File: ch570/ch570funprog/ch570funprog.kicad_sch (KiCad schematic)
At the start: 19 parts, among them J1 DEVPGM, J2 USB_C_Receptacle_USB2.0, J3 COREPGM, U1 USBLC6-2SC6, U2 CH570Q, U3 AMS1117-3.3, U4 DMC2400UV, Y1 32M

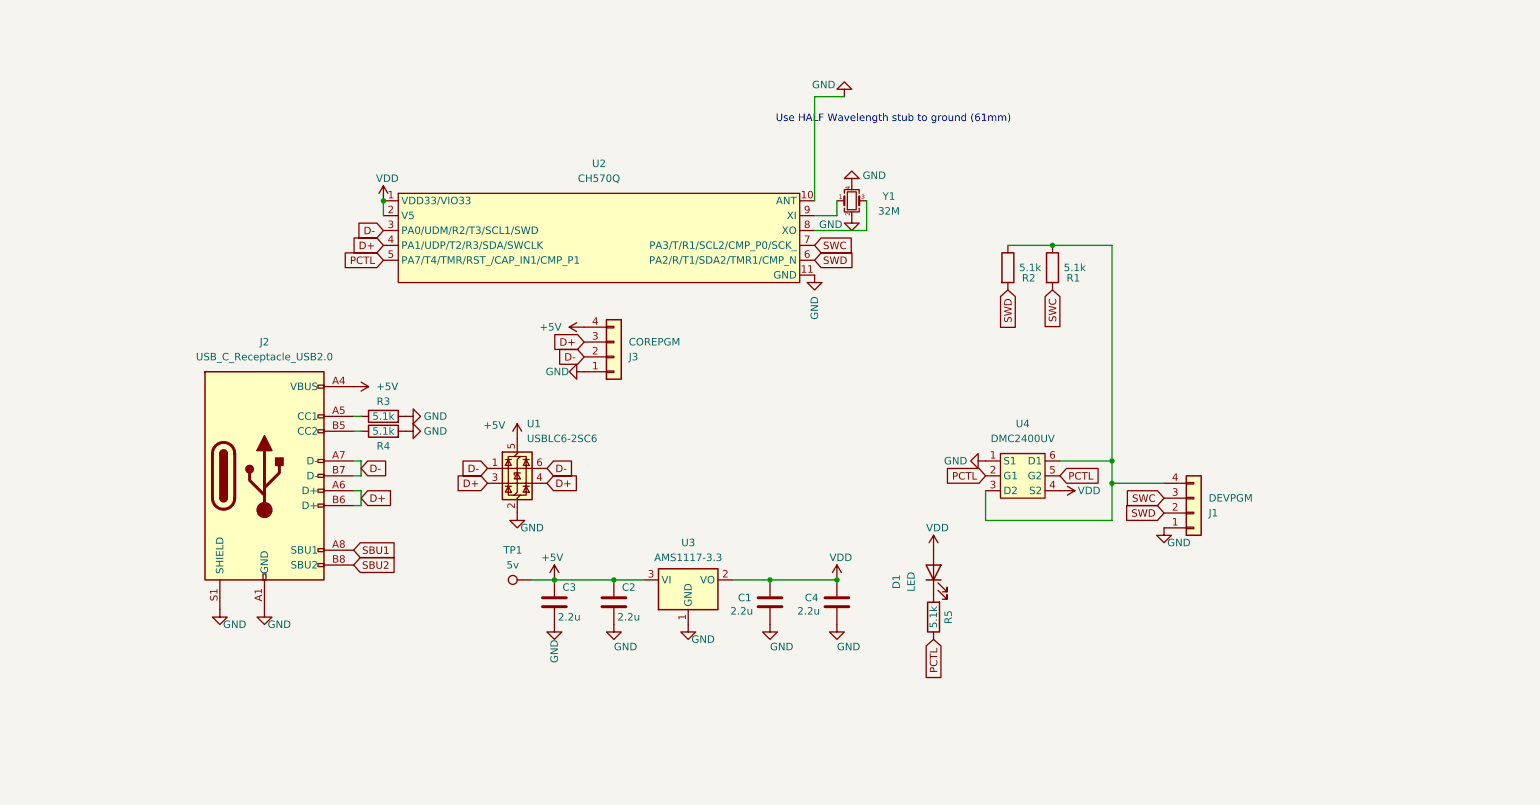
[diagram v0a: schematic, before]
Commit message: Bump design workAnd properly name polypsec
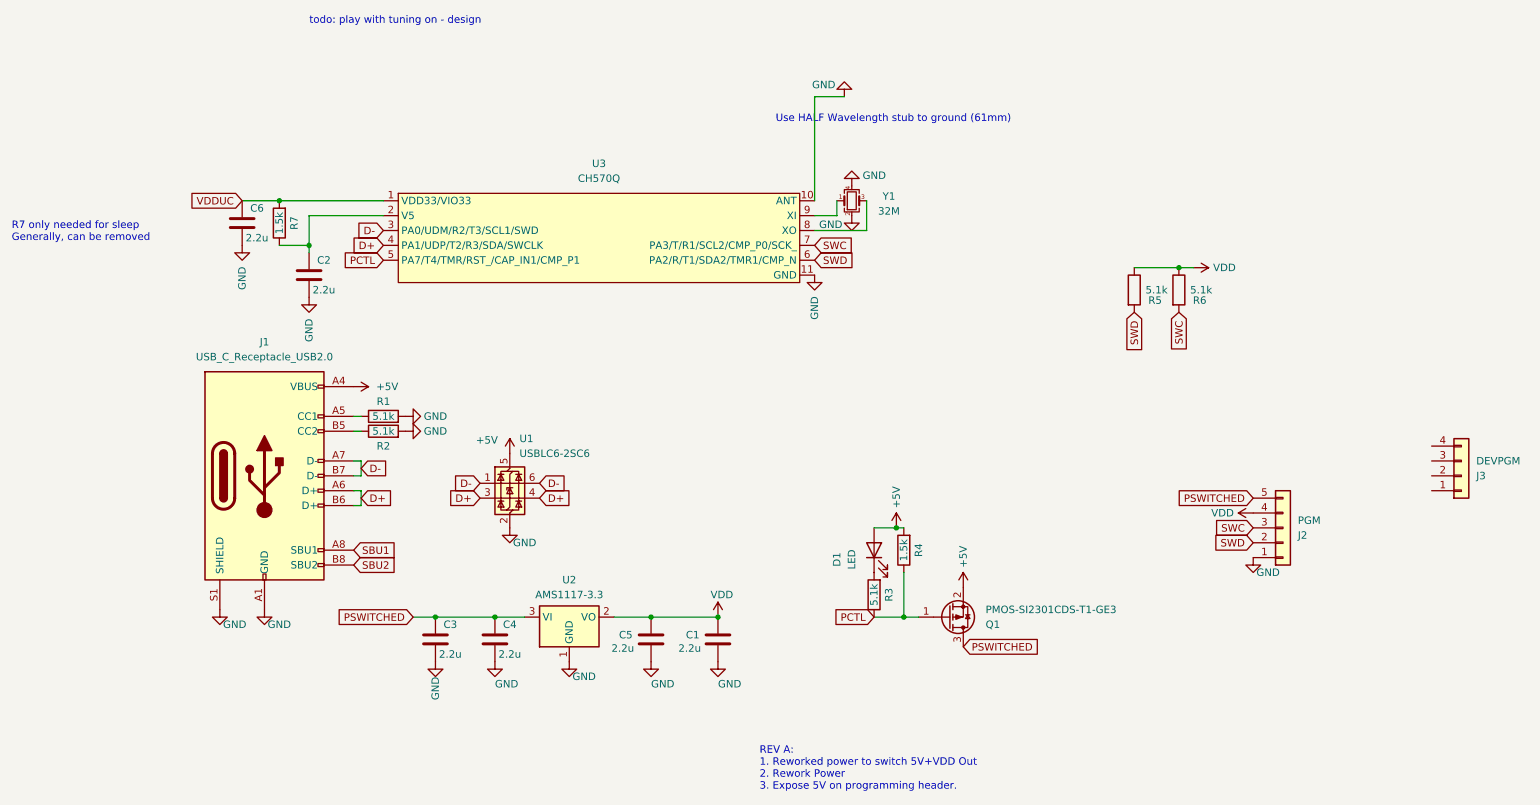
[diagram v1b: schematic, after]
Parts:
- removed J3: COREPGM, Connector_PinHeader_2.54mm:PinHeader_1x04_P2.54mm_Vertical, symbol Connector_Generic:Conn_01x04
- removed TP1: 5v, TestPoint:TestPoint_Pad_D1.5mm, symbol Connector:TestPoint
- removed U4: DMC2400UV, Package_TO_SOT_SMD:SOT-563, symbol cnhardware:DMC2400UV_COMPLEMENTARY_PAIR_FET
- added C2, C6: 2.2u, Resistor_SMD:R_0402_1005Metric, symbol Device:C
- added J2: PGM, Connector_PinHeader_2.54mm:PinHeader_1x05_P2.54mm_Horizontal, symbol Connector_Generic:Conn_01x05
- added Q1: PMOS-SI2301CDS-T1-GE3, Package_TO_SOT_SMD:SOT-23, symbol Transistor_FET:Q_PMOS_GSD
- added R4, R7: 1.5k, Resistor_SMD:R_0402_1005Metric, symbol Device:R
- renumbered C4 to C1, C2 to C4, C1 to C5, J2 to J1, J1 to J3, R3 to R1, R4 to R2, R5 to R3, R2 to R5, R1 to R6, U3 to U2, U2 to U3
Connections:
- net +5V: now also D1.2 (A), Q1.2 (S), R4.2; no longer C3.2, C4.2, U2.3 (VI)
- net GND: now also C2.1, C6.1, J2.1 (Pin_1); no longer J3.1 (Pin_1)
- net PCTL: now also Q1.1 (G), R4.1
- net SWC: now also J2.3 (Pin_3); no longer J3.3 (Pin_3)
- net SWD: now also J2.2 (Pin_2); no longer J3.2 (Pin_2)
- net VDD: now also R5.1, R6.1, J2.4 (Pin_4); no longer D1.2 (A), U3.1 (VDD33/VIO33), U3.2 (V5)
- new net: C2.2, R7.1, U3.2 (V5)
- new net PSWITCHED: C3.2, C4.2, J2.5 (Pin_5), Q1.3 (D), U2.3 (VI)
- new net VDDUC: C6.2, R7.2, U3.1 (VDD33/VIO33)
- now unconnected: J3.4 (Pin_4)
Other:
- note added: "R7 only needed for sleep Generally, can be removed"
- note added: "REV A: 1. Reworked power to switch 5V+VDD Out 2. Rework Power 3. Expose 5V on programming header."
- note added: "todo: play with tuning on - design"
- moved on the sheet: C1, C3, C4, C5, D1, J3, R3, R5, R6, U1, U2
